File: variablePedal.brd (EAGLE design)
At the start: 100 x 80 mm, 16 parts, among them IC1 OPA340U, J2 AUDIO_JACK_TRS_0.25"_PTH_RA, J3 AUDIO_JACK_TRS_0.25"_PTH_RA, J4 5.5x2.1mm Barrel, Q1 MPSA56

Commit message: parts placed
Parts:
- moved R1 88.9 mm to (36.8, 25.4)
- moved C2 86.7 mm to (34.3, 35.6), turned to 90 degrees
- moved C1 81.3 mm to (25.4, 12.7), turned to 270 degrees
- moved J3 80.2 mm to (36.8, 58.4), turned to 180 degrees
- moved C3 76.7 mm to (20.3, 43.2), turned to 270 degrees
- moved TM1 64.3 mm to (27.9, 33.0)
- moved Q1 57.5 mm to (21.6, 25.4)
- moved TM2 57.1 mm to (14.0, 33.0)
- moved R3 53.1 mm to (34.3, 43.2), turned to 90 degrees
- moved J4 52.1 mm to (3.81, 44.5)
- moved IC1 47.1 mm to (27.9, 43.2), turned to 180 degrees
- moved J2 45.7 mm to (8.89, 8.89)
- moved R5 44.2 mm to (16.5, 48.3), turned to 90 degrees
- moved R4 43.3 mm to (16.5, 39.4), turned to 90 degrees
- moved R6 40.9 mm to (6.35, 59.7)
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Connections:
- net V+: now also J4.GND
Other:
- board size 100 x 80 mm -> 42.9 x 67.3 mm

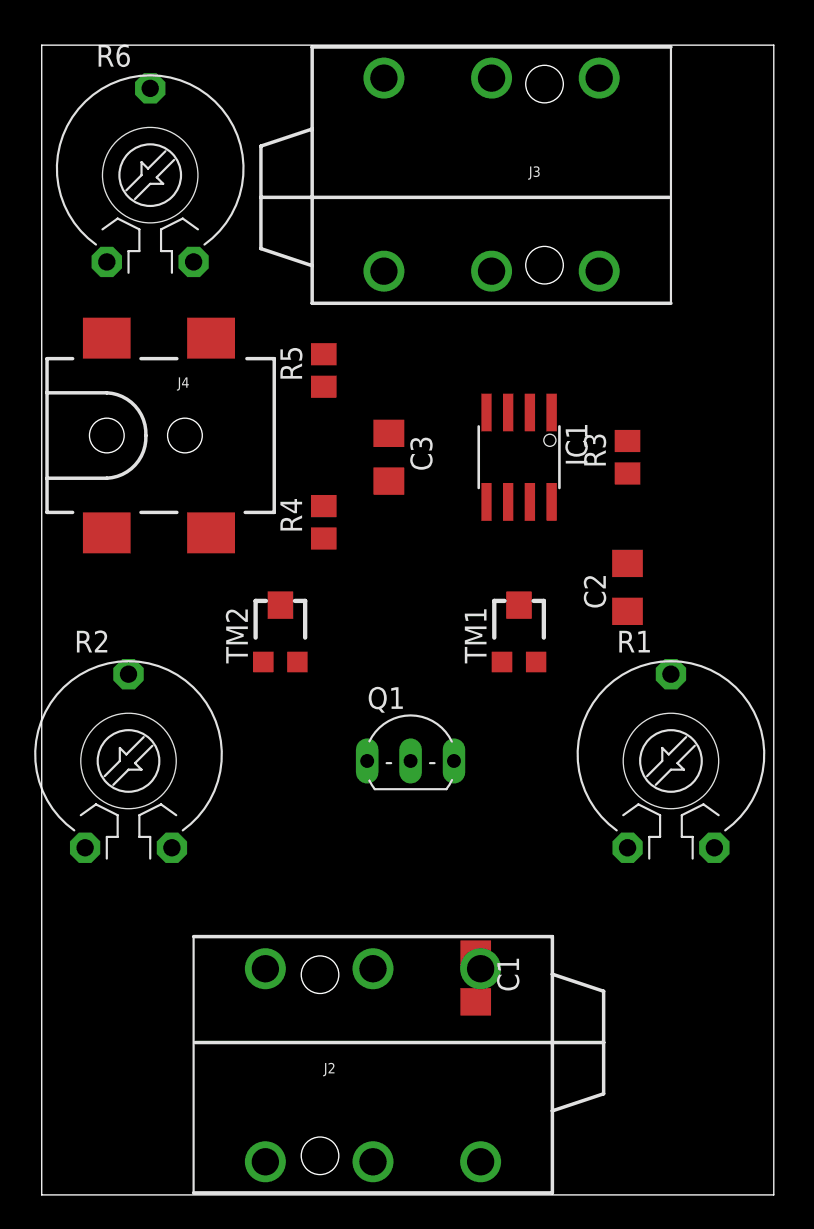
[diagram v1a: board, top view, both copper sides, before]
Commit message: Passes DRC with no errors, however, BJT holder TBD
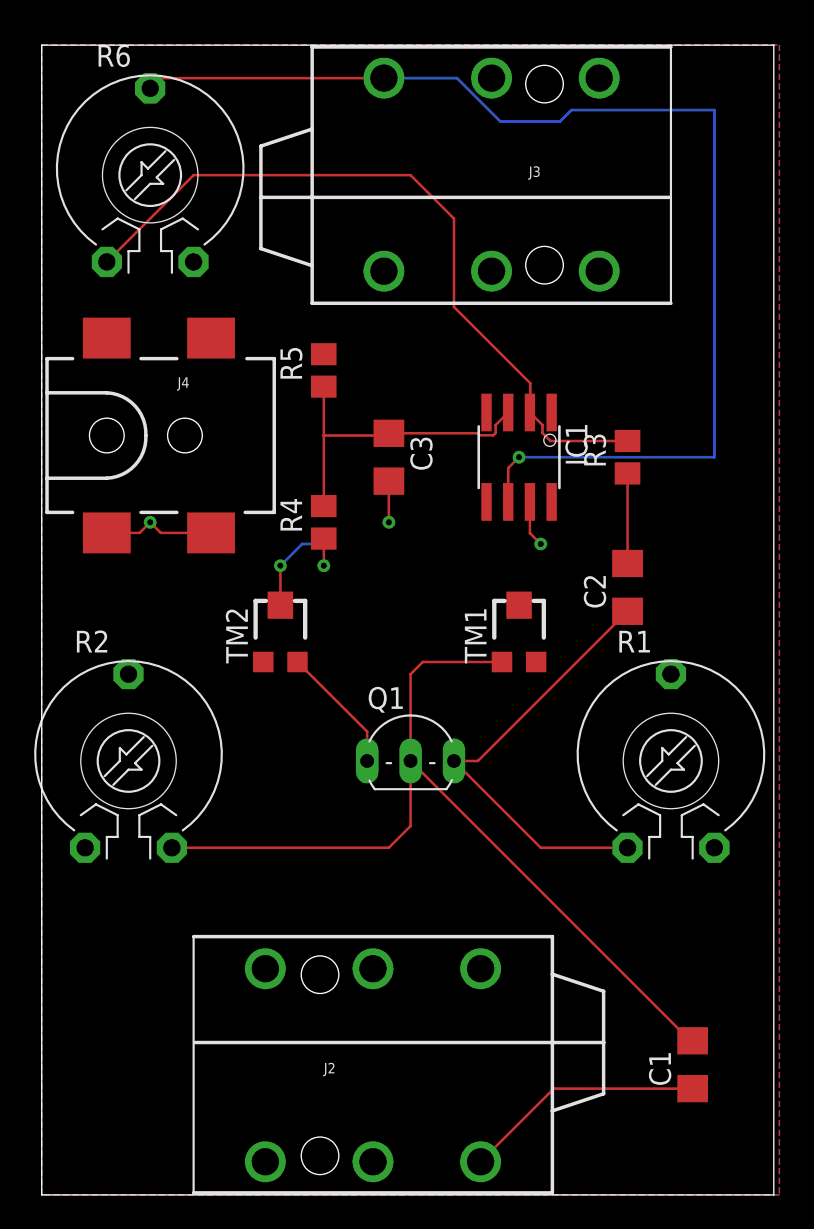
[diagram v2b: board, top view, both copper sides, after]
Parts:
- moved C1 13.7 mm to (38.1, 7.62), turned to 90 degrees
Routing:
- net N$7: track 0.00 -> 69.2 mm, vias 0 -> 1
- net N$1: track 0.00 -> 52.3 mm
- net N$6: track 0.00 -> 43.4 mm
- net N$2: track 0.00 -> 26.1 mm
- net V+: track 0.00 -> 18.7 mm, vias 0 -> 5
- net N$5: track 0.00 -> 18.7 mm
- net N$11: track 0.00 -> 14.2 mm
- net N$3: track 0.00 -> 7.48 mm
- net N$4: track 0.00 -> 5.27 mm
- added copper zone on layer 1, net GND
- added copper zone on layer 16, net V+

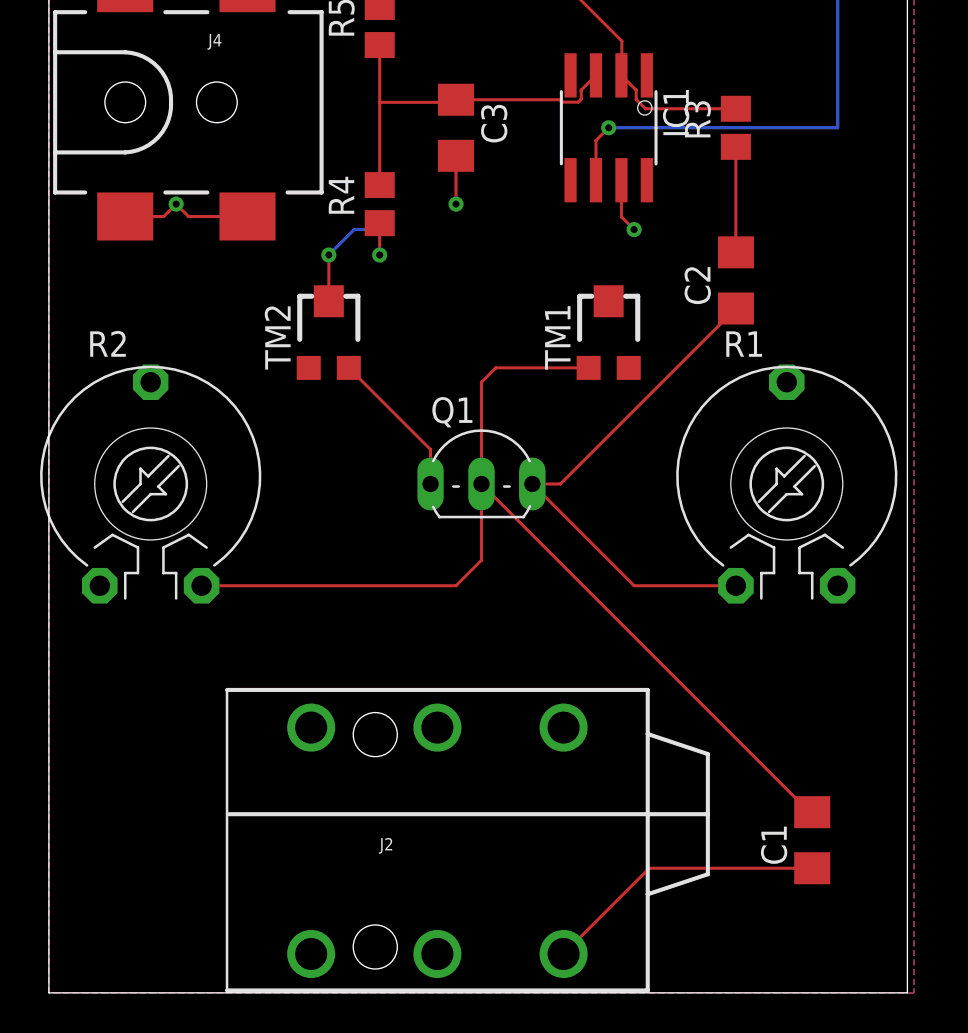
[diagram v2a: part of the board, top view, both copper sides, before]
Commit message: Some finishing touches (labels, tidy placement)
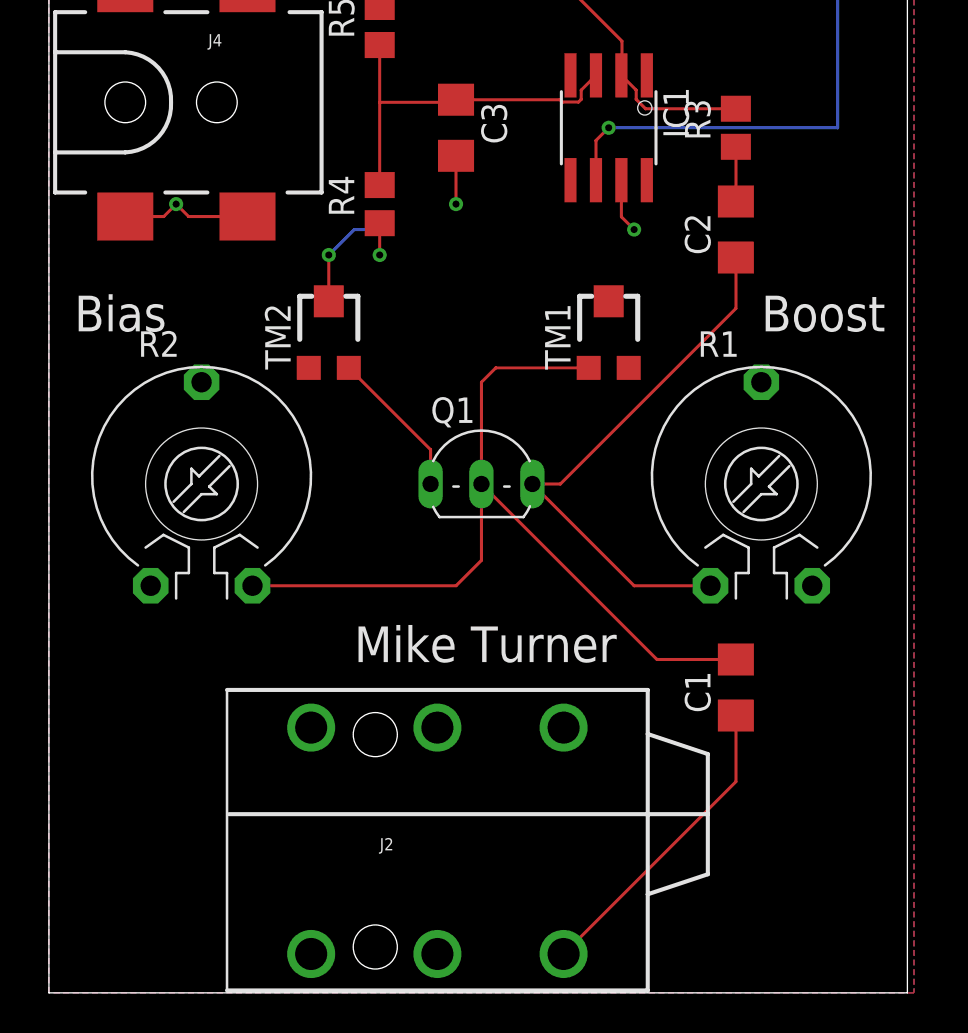
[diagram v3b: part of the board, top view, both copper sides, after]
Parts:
- moved C1 8.52 mm to (34.3, 15.2)
- moved R2 2.54 mm to (7.62, 25.4)
- moved C2 2.54 mm to (34.3, 38.1)
- moved R1 1.27 mm to (35.6, 25.4)
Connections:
- net GND: now also J2.SLEEVE-NORM
- net N$11: now also J2.TIP-NORM
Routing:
- net N$1: track 52.3 -> 42.8 mm
- net N$4: track 5.27 -> 2.73 mm
- net N$11: track 14.2 -> 15.5 mm
- net N$2: track 26.1 -> 27.3 mm
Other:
- board text added: "Bias"
- board text added: "Boost"
- board text added: "Mike Turner"

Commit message: Revert "Some finishing touches (labels, tidy placement)"
This reverts commit a6e963cb4720da940ed62cc4250a87c95adb02c4.
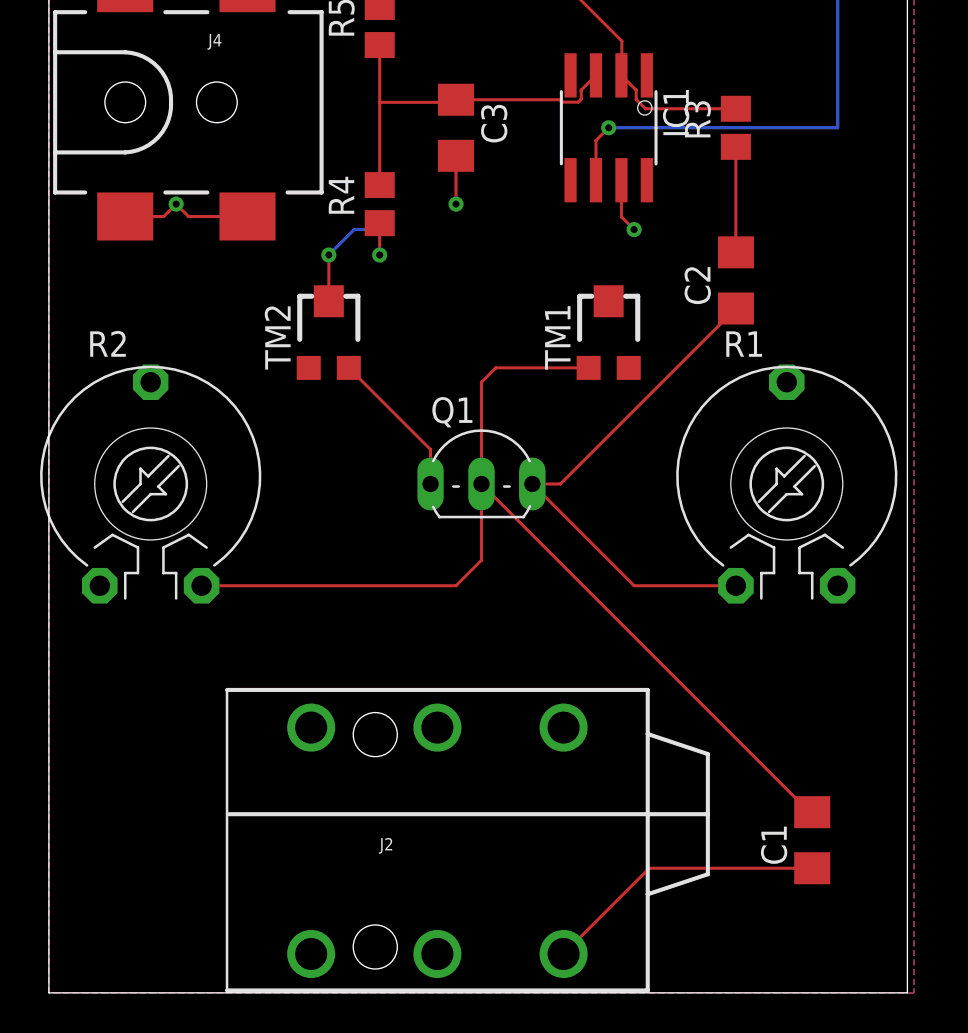
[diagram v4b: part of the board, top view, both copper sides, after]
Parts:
- moved C1 8.52 mm to (38.1, 7.62)
- moved R2 2.54 mm to (5.08, 25.4)
- moved C2 2.54 mm to (34.3, 35.6)
- moved R1 1.27 mm to (36.8, 25.4)
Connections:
- net GND: no longer J2.SLEEVE-NORM
- net N$11: no longer J2.TIP-NORM
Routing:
- net N$1: track 42.8 -> 52.3 mm
- net N$4: track 2.73 -> 5.27 mm
- net N$11: track 15.5 -> 14.2 mm
- net N$2: track 27.3 -> 26.1 mm
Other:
- board text removed: "Bias"
- board text removed: "Boost"
- board text removed: "Mike Turner"

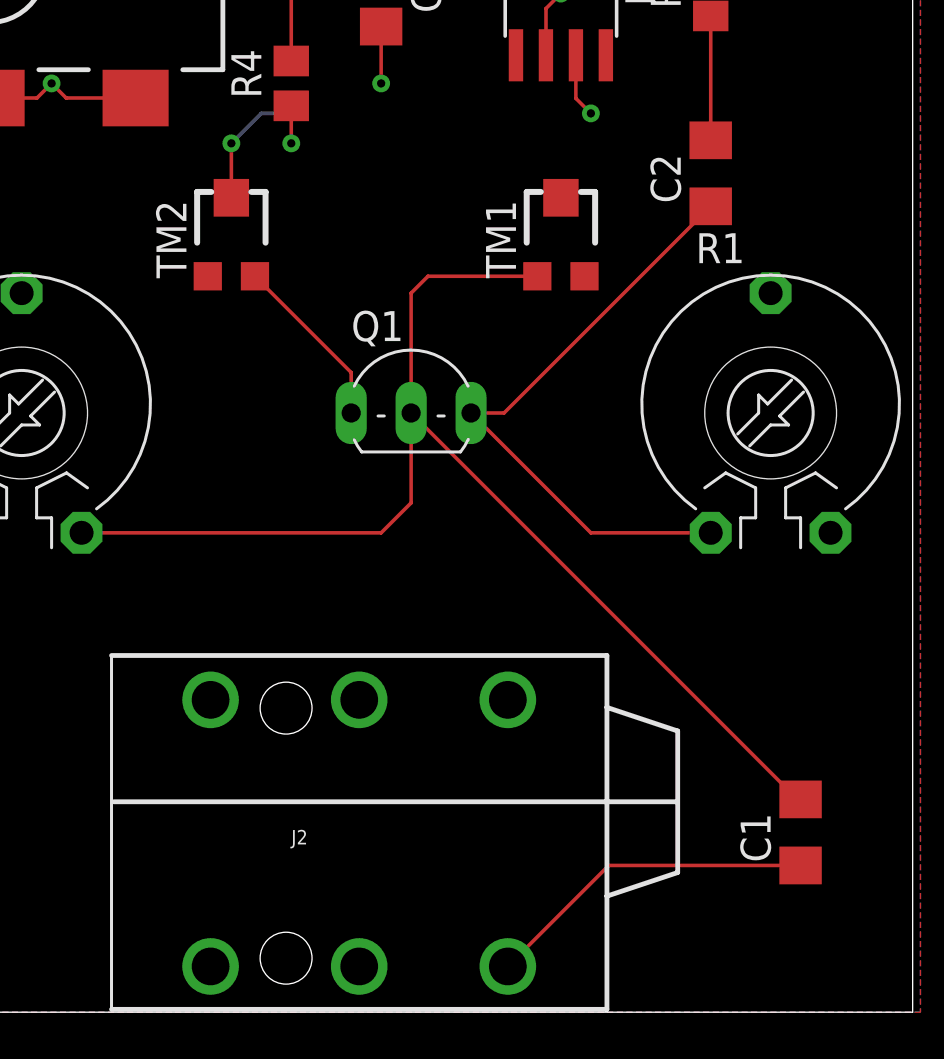
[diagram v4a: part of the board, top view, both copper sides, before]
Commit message: Some finishing touches (labels, tidy placement)
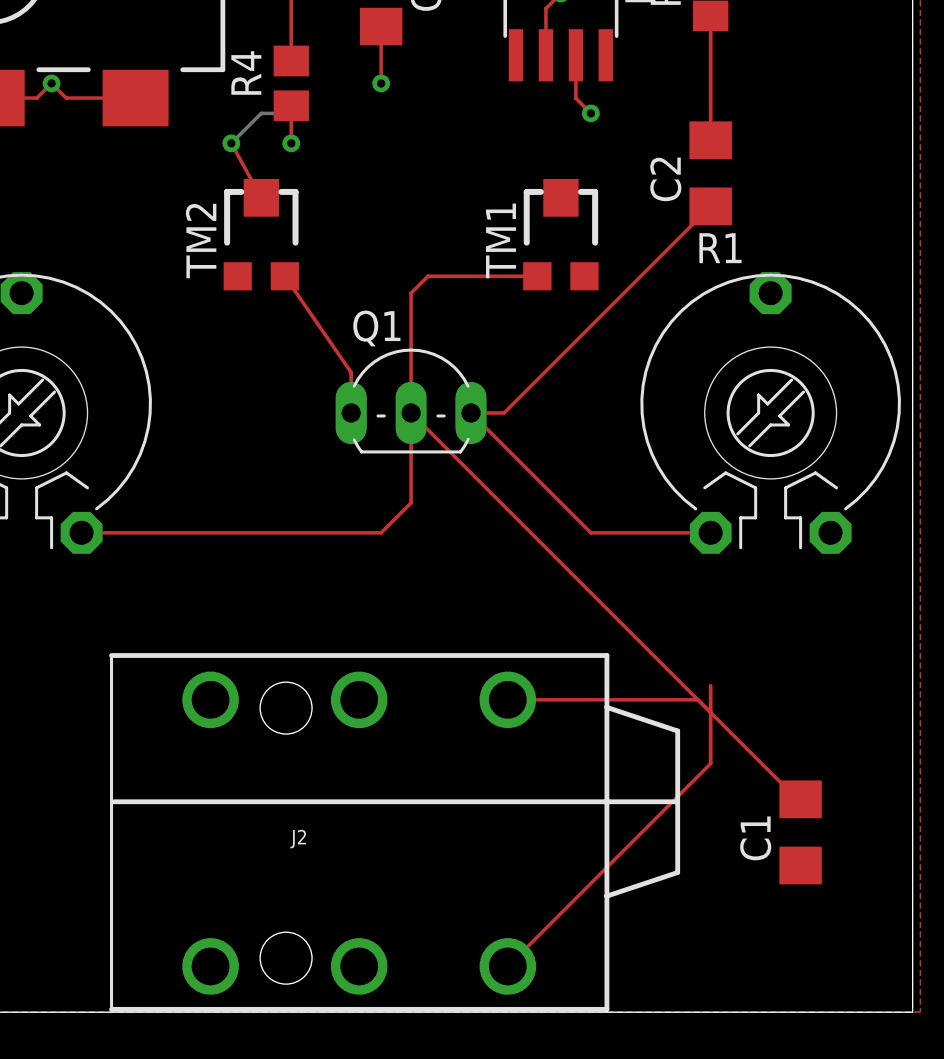
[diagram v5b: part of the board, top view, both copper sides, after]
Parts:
- moved TM2 1.27 mm to (15.2, 33.0)
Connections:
- net GND: now also J2.SLEEVE-NORM
- net N$11: now also J2.TIP-NORM
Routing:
- net N$11: track 14.2 -> 24.3 mm
- net N$3: track 7.48 -> 6.67 mm
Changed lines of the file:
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@@
 <attribute name="VALUE" x="31.115" y="31.115" size="1.27" layer="27" rot="R90"/>
 </element>
-<element name="TM2" library="adafruit" library_urn="urn:adsk.eagle:library:420" package="TC33X" package3d_urn="urn:adsk.eagle:package:6240639/1" value="" x="13.97" y="33.02" smashed="yes">
-<attribute name="NAME" x="12.065" y="31.115" size="1.27" layer="25" rot="R90"/>
-<attribute name="VALUE" x="17.145" y="31.115" size="1.27" layer="27" rot="R90"/>
+<element name="TM2" library="adafruit" library_urn="urn:adsk.eagle:library:420" package="TC33X" package3d_urn="urn:adsk.eagle:package:6240639/1" value="" x="15.24" y="33.02" smashed="yes">
+<attribute name="NAME" x="13.335" y="31.115" size="1.27" layer="25" rot="R90"/>
+<attribute name="VALUE" x="18.415" y="31.115" size="1.27" layer="27" rot="R90"/>
 </element>
 </elements>
@@
 <vertex x="43.18" y="0"/>
 </polygon>
+<contactref element="J2" pad="SLEEVE-NORM"/>
 </signal>
 <signal name="N$2">
@@
 <contactref element="Q1" pad="E"/>
 <contactref element="TM2" pad="3"/>
-<wire x1="14.97" y1="31.195" x2="19.05" y2="27.115" width="0.1524" layer="1"/>
+<wire x1="16.24" y1="31.195" x2="19.05" y2="27.115" width="0.1524" layer="1"/>
 <wire x1="19.05" y1="27.115" x2="19.05" y2="25.4" width="0.1524" layer="1"/>
 </signal>
@@
 <wire x1="9.91" y1="38.75" x2="6.97" y2="38.75" width="0.1524" layer="1"/>
 <wire x1="6.97" y1="38.75" x2="6.35" y2="39.37" width="0.1524" layer="1"/>
-<wire x1="13.97" y1="34.52" x2="13.97" y2="36.83" width="0.1524" layer="1"/>
+<wire x1="15.24" y1="34.52" x2="13.97" y2="36.83" width="0.1524" layer="1"/>
 <via x="13.97" y="36.83" extent="1-16" drill="0.35"/>
 <wire x1="13.97" y1="36.83" x2="15.24" y2="38.1" width="0.1524" layer="16"/>
@@
 <contactref element="J2" pad="TIP"/>
 <contactref element="C1" pad="1"/>
-<wire x1="25.69" y1="1.94" x2="29.97" y2="6.22" width="0.1524" layer="1"/>
-<wire x1="29.97" y1="6.22" x2="38.1" y2="6.22" width="0.1524" layer="1"/>
+<wire x1="25.69" y1="1.94" x2="34.29" y2="10.54" width="0.1524" layer="1"/>
+<wire x1="34.29" y1="10.54" x2="34.29" y2="12.7" width="0.1524" layer="1"/>
+<contactref element="J2" pad="TIP-NORM"/>
+<wire x1="34.29" y1="12.7" x2="34.29" y2="13.84" width="0.1524" layer="1"/>
+<wire x1="25.69" y1="13.24" x2="33.75" y2="13.24" width="0.1524" layer="1"/>
+<wire x1="33.75" y1="13.24" x2="34.29" y2="12.7" width="0.1524" layer="1"/>
 </signal>
 </signals>

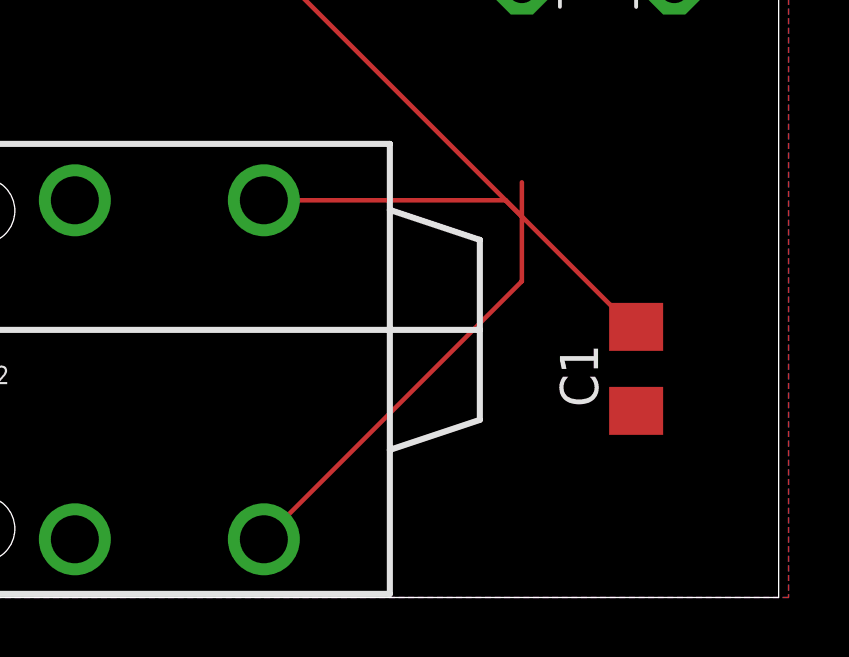
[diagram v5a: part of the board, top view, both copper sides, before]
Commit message: fixed trace collision
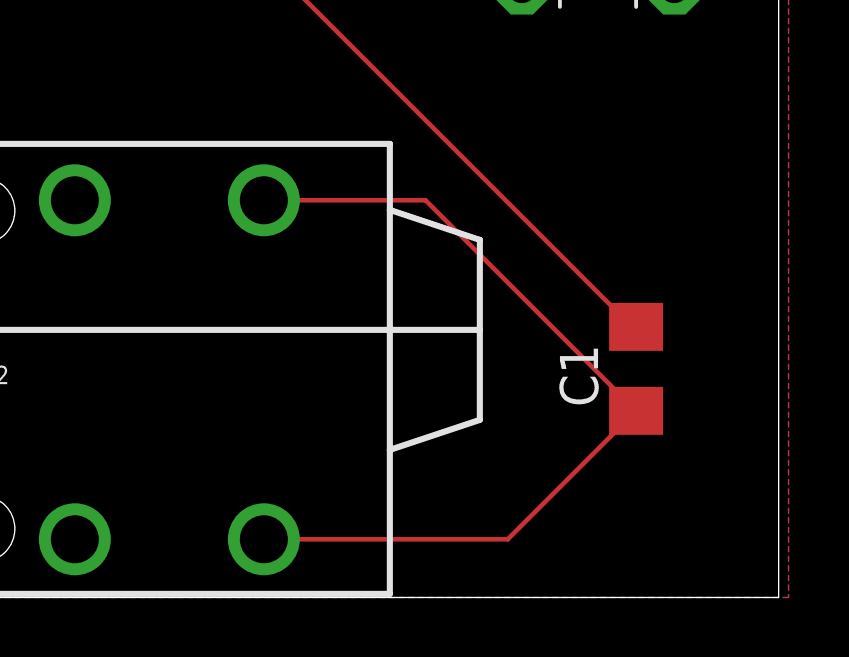
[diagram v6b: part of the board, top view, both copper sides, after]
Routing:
- net N$11: track 24.3 -> 29.5 mm
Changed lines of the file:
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@@
 <contactref element="J2" pad="TIP"/>
 <contactref element="C1" pad="1"/>
-<wire x1="25.69" y1="1.94" x2="34.29" y2="10.54" width="0.1524" layer="1"/>
-<wire x1="34.29" y1="10.54" x2="34.29" y2="12.7" width="0.1524" layer="1"/>
 <contactref element="J2" pad="TIP-NORM"/>
-<wire x1="34.29" y1="12.7" x2="34.29" y2="13.84" width="0.1524" layer="1"/>
-<wire x1="25.69" y1="13.24" x2="33.75" y2="13.24" width="0.1524" layer="1"/>
-<wire x1="33.75" y1="13.24" x2="34.29" y2="12.7" width="0.1524" layer="1"/>
+<wire x1="25.69" y1="13.24" x2="31.08" y2="13.24" width="0.1524" layer="1"/>
+<wire x1="31.08" y1="13.24" x2="38.1" y2="6.22" width="0.1524" layer="1"/>
+<wire x1="25.69" y1="1.94" x2="33.82" y2="1.94" width="0.1524" layer="1"/>
+<wire x1="33.82" y1="1.94" x2="38.1" y2="6.22" width="0.1524" layer="1"/>
 </signal>
 </signals>
